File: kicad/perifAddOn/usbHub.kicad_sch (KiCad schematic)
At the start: 38 parts, among them J2 105450-0101, SW1 B3U-1000P[], U1 USB2513B-AEZC, U13 NCP1529A, U4 SN74HC266DR, X1 ECS-2520MV-240-BL-TR

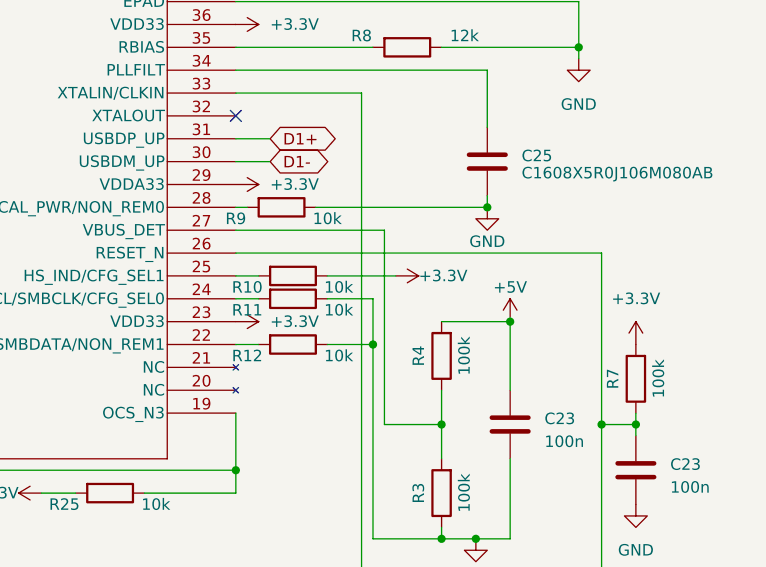
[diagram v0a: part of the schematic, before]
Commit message: V1.1 of perifAddOn (added bus-switch on sd-card)
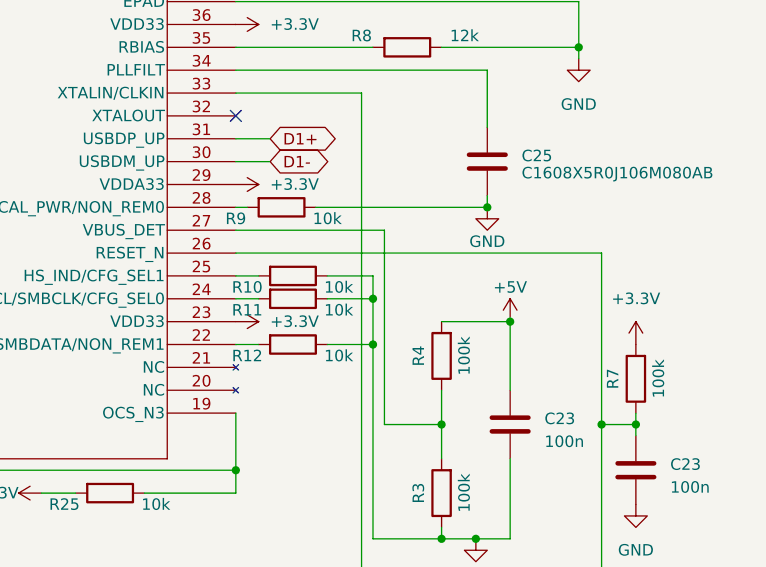
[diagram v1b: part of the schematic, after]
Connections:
- net +3.3V: no longer R10.1
- net GND: now also R10.1
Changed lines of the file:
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@@
   (junction (at 147.32 161.29) (diameter 0) (color 0 0 0 0)
+  )
+  (junction (at 243.84 63.5) (diameter 0) (color 0 0 0 0)
   )
   (junction (at 76.2 49.53) (diameter 0) (color 0 0 0 0)
@@
     (stroke (width 0) (type default))
   )
-  (wire (pts (xy 238.76 60.96) (xy 246.38 60.96))
-    (stroke (width 0) (type default))
-  )
   (wire (pts (xy 245.11 55.88) (xy 245.11 77.47))
     (stroke (width 0) (type default))
@@
     (stroke (width 0) (type default))
   )
+  (wire (pts (xy 238.76 60.96) (xy 243.84 60.96))
+    (stroke (width 0) (type default))
+  )
   (wire (pts (xy 251.46 66.04) (xy 259.08 66.04))
     (stroke (width 0) (type default))
@@
   )
   (wire (pts (xy 116.84 153.67) (xy 119.38 153.67))
+    (stroke (width 0) (type default))
+  )
+  (wire (pts (xy 243.84 60.96) (xy 243.84 63.5))
     (stroke (width 0) (type default))
   )
@@
       )
       (project "perifAddOn"
-        (path "/c4a49e8d-4344-49ad-8b55-370a9310fd4c"
-          (reference "#PWR02") (unit 1)
-        )
         (path "/c4a49e8d-4344-49ad-8b55-370a9310fd4c/864ac336-bbc9-4ed3-a54d-59ff29ebf05e"
           (reference "#PWR027") (unit 1)
@@
         (path "/c4a49e8d-4344-49ad-8b55-370a9310fd4c/864ac336-bbc9-4ed3-a54d-59ff29ebf05e"
           (reference "C14") (unit 1)
-        )
-      )
-    )
-  )
-  (symbol (lib_id "power:+3.3V") (at 246.38 60.96 270) (unit 1)
-    (in_bom yes) (on_board yes) (dnp no)
-    (property "Reference" "#PWR091" (at 242.57 60.96 0)
-      (effects (font (size 1.27 1.27)) hide)
-    )
-    (property "Value" "+3.3V" (at 248.92 60.96 90)
-      (effects (font (size 1.27 1.27)) (justify left))
-    )
-    (property "Footprint" "" (at 246.38 60.96 0)
-      (effects (font (size 1.27 1.27)) hide)
-    )
-    (property "Datasheet" "" (at 246.38 60.96 0)
-      (effects (font (size 1.27 1.27)) hide)
-    )
-    (pin "1")
-    (instances
-      (project "gecko5education"
-        (path "/47d58937-9286-45a8-b88f-d3fcc6f916c8/1b790ed2-2ed7-44b0-8848-0151372cb9f5"
-          (reference "#PWR091") (unit 1)
-        )
-      )
-      (project "cpuAddOn"
-        (path "/9e68661c-b1e3-4cc9-aa9a-0ec357e0a727"
-          (reference "#PWR02") (unit 1)
-        )
-        (path "/9e68661c-b1e3-4cc9-aa9a-0ec357e0a727/dc9ec033-7c25-4719-8793-b075d3f8af9a"
-          (reference "#PWR026") (unit 1)
-        )
-      )
-      (project "perifAddOn"
-        (path "/c4a49e8d-4344-49ad-8b55-370a9310fd4c"
-          (reference "#PWR02") (unit 1)
-        )
-        (path "/c4a49e8d-4344-49ad-8b55-370a9310fd4c/864ac336-bbc9-4ed3-a54d-59ff29ebf05e"
-          (reference "#PWR029") (unit 1)
         )
       )
@@
       )
       (project "perifAddOn"
-        (path "/c4a49e8d-4344-49ad-8b55-370a9310fd4c"
-          (reference "#PWR01") (unit 1)
-        )
         (path "/c4a49e8d-4344-49ad-8b55-370a9310fd4c/864ac336-bbc9-4ed3-a54d-59ff29ebf05e"
           (reference "#PWR033") (unit 1)
@@
       )
       (project "perifAddOn"
-        (path "/c4a49e8d-4344-49ad-8b55-370a9310fd4c"
-          (reference "#PWR02") (unit 1)
-        )
         (path "/c4a49e8d-4344-49ad-8b55-370a9310fd4c/864ac336-bbc9-4ed3-a54d-59ff29ebf05e"
           (reference "#PWR015") (unit 1)
@@
       )
       (project "perifAddOn"
-        (path "/c4a49e8d-4344-49ad-8b55-370a9310fd4c"
-          (reference "#PWR02") (unit 1)
-        )
         (path "/c4a49e8d-4344-49ad-8b55-370a9310fd4c/864ac336-bbc9-4ed3-a54d-59ff29ebf05e"
           (reference "#PWR026") (unit 1)
@@
       )
       (project "perifAddOn"
-        (path "/c4a49e8d-4344-49ad-8b55-370a9310fd4c"
-          (reference "#PWR02") (unit 1)
-        )
         (path "/c4a49e8d-4344-49ad-8b55-370a9310fd4c/864ac336-bbc9-4ed3-a54d-59ff29ebf05e"
           (reference "#PWR035") (unit 1)
@@
       )
       (project "perifAddOn"
-        (path "/c4a49e8d-4344-49ad-8b55-370a9310fd4c"
-          (reference "#PWR02") (unit 1)
-        )
         (path "/c4a49e8d-4344-49ad-8b55-370a9310fd4c/864ac336-bbc9-4ed3-a54d-59ff29ebf05e"
           (reference "#PWR025") (unit 1)
@@
       )
       (project "perifAddOn"
-        (path "/c4a49e8d-4344-49ad-8b55-370a9310fd4c"
-          (reference "#PWR02") (unit 1)
-        )
         (path "/c4a49e8d-4344-49ad-8b55-370a9310fd4c/864ac336-bbc9-4ed3-a54d-59ff29ebf05e"
           (reference "#PWR016") (unit 1)
@@
       )
       (project "perifAddOn"
-        (path "/c4a49e8d-4344-49ad-8b55-370a9310fd4c"
-          (reference "#PWR02") (unit 1)
-        )
         (path "/c4a49e8d-4344-49ad-8b55-370a9310fd4c/864ac336-bbc9-4ed3-a54d-59ff29ebf05e"
           (reference "#PWR024") (unit 1)
@@
       )
       (project "perifAddOn"
-        (path "/c4a49e8d-4344-49ad-8b55-370a9310fd4c"
-          (reference "#PWR02") (unit 1)
-        )
         (path "/c4a49e8d-4344-49ad-8b55-370a9310fd4c/864ac336-bbc9-4ed3-a54d-59ff29ebf05e"
           (reference "#PWR012") (unit 1)
@@
       )
       (project "perifAddOn"
-        (path "/c4a49e8d-4344-49ad-8b55-370a9310fd4c"
-          (reference "#PWR02") (unit 1)
-        )
         (path "/c4a49e8d-4344-49ad-8b55-370a9310fd4c/864ac336-bbc9-4ed3-a54d-59ff29ebf05e"
           (reference "#PWR017") (unit 1)
